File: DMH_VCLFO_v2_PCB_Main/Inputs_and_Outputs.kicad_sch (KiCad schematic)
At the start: 61 parts, among them J1 TS_Jack_6.35mm_Sw, J10 IDC_02x05, J19 Conn_01x08, J2 TS_Jack_6.35mm_Sw, J3 TS_Jack_6.35mm_Sw, J4 TS_Jack_6.35mm_Sw, J5 TS_Jack_6.35mm_Sw, J6 TS_Jack_6.35mm_Sw, J7 Conn_01x08, J8 Conn_01x08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

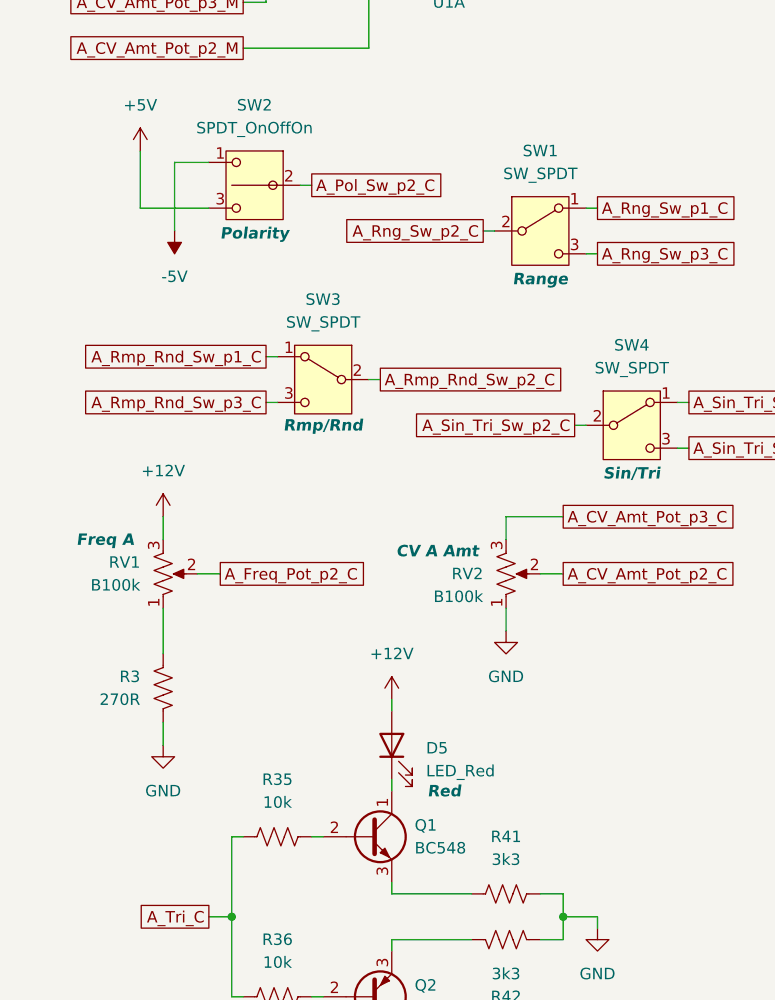
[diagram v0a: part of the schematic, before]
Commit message: Designed osc core based on slew module
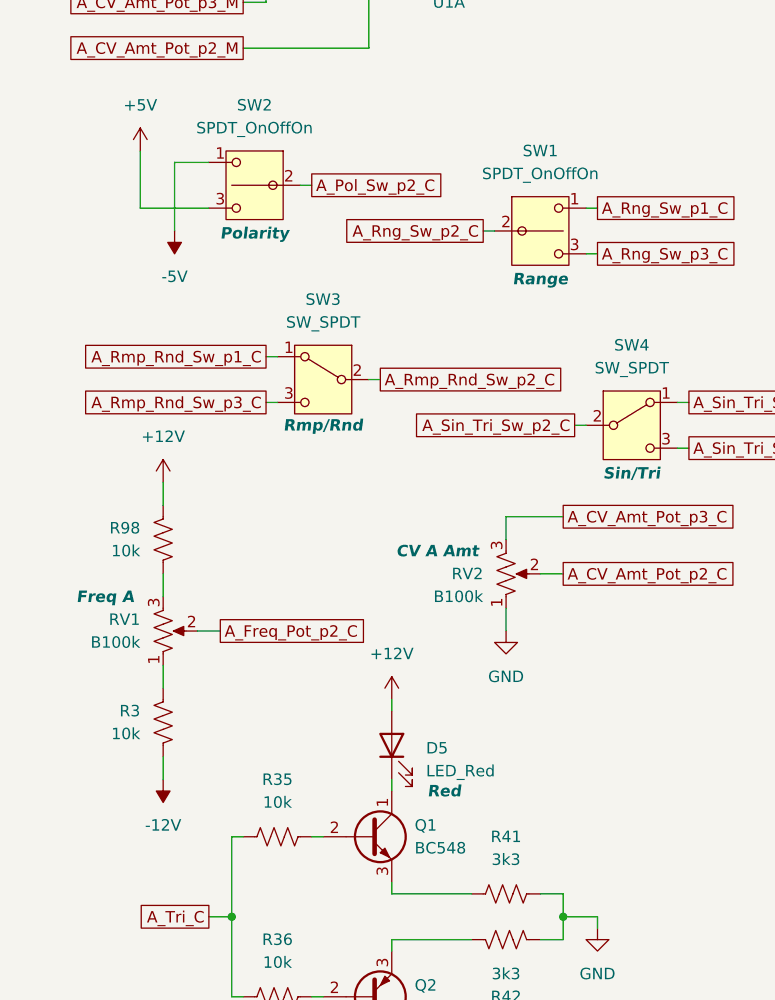
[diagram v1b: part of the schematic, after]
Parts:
- added R98: 10k, Resistor_THT:R_Axial_DIN0207_L6.3mm_D2.5mm_P7.62mm_Horizontal, symbol Device:R_US
- R3: value 270R -> 10k
- SW1: value SW_SPDT -> SPDT_OnOffOn; symbol Switch:SW_SPDT -> SynthStuff:SW_SPDT_OnOffOn
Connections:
- net +12V: now also R98.1; no longer RV1.3
- net -12V: now also R3.2
- net GND: no longer R3.2
- new net: R98.2, RV1.3
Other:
- moved on the sheet: R3, RV1
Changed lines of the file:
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@@
 	(wire
 		(pts
-			(xy 25.4 137.16) (xy 25.4 139.7)
+			(xy 25.4 140.97) (xy 25.4 143.51)
 		)
 		(stroke
@@
 	(wire
 		(pts
+			(xy 25.4 120.65) (xy 25.4 123.19)
+		)
+		(stroke
+			(width 0)
+			(type default)
+		)
+	)
+	(wire
+		(pts
 			(xy 50.8 156.21) (xy 50.8 154.94)
 		)
@@
 	(wire
 		(pts
-			(xy 25.4 114.3) (xy 25.4 116.84)
+			(xy 25.4 110.49) (xy 25.4 113.03)
 		)
 		(stroke
@@
 	(wire
 		(pts
-			(xy 29.21 120.65) (xy 31.75 120.65)
+			(xy 29.21 127) (xy 31.75 127)
 		)
 		(stroke
@@
 	(wire
 		(pts
-			(xy 25.4 124.46) (xy 25.4 129.54)
+			(xy 25.4 130.81) (xy 25.4 133.35)
 		)
 		(stroke
@@
 	(global_label "A_Freq_Pot_p2_C"
 		(shape passive)
-		(at 31.75 120.65 0)
+		(at 31.75 127 0)
 		(fields_autoplaced yes)
 		(effects
@@
 		)
 		(property "Intersheetrefs" "${INTERSHEET_REFS}"
-			(at 49.4685 120.65 0)
+			(at 49.4685 127 0)
 			(effects
 				(font
@@
 	(symbol
 		(lib_id "Device:R_US")
+		(at 25.4 116.84 0)
+		(mirror y)
+		(unit 1)
+		(exclude_from_sim no)
+		(in_bom yes)
+		(on_board no)
+		(dnp no)
+		(property "Reference" "R98"
+			(at 22.86 115.5699 0)
+			(effects
+				(font
+					(size 1.27 1.27)
+				)
+				(justify left)
+			)
+		)
+		(property "Value" "10k"
+			(at 22.86 118.1099 0)
+			(effects
+				(font
+					(size 1.27 1.27)
+				)
+				(justify left)
+			)
+		)
+		(property "Footprint" "Resistor_THT:R_Axial_DIN0207_L6.3mm_D2.5mm_P7.62mm_Horizontal"
+			(at 24.384 117.094 90)
+			(effects
+				(font
+					(size 1.27 1.27)
+				)
+				(hide yes)
+			)
+		)
+		(property "Datasheet" "~"
+			(at 25.4 116.84 0)
+			(effects
+				(font
+					(size 1.27 1.27)
+				)
+				(hide yes)
+			)
+		)
+		(property "Description" "Resistor, US symbol"
+			(at 25.4 116.84 0)
+			(effects
+				(font
+					(size 1.27 1.27)
+				)
+				(hide yes)
+			)
+		)
+		(property "Function" ""
+			(at 25.4 116.84 0)
+			(effects
+				(font
+					(size 1.27 1.27)
+				)
+			)
+		)
+		(pin "1"
+		)
+		(pin "2"
+		)
+		(instances
+			(project "DMH_VCLFO_v2_PCB_Main"
+				(path "/58f4306d-5387-4983-bb08-41a2313fd315/ce3fef8b-9f1d-4178-b50b-4a046c030679"
+					(reference "R98")
+					(unit 1)
+				)
+			)
+		)
+	)
+	(symbol
+		(lib_id "Device:R_US")
 		(at 125.73 139.7 90)
 		(unit 1)
@@
 	)
 	(symbol
-		(lib_id "power:GND")
-		(at 25.4 139.7 0)
-		(unit 1)
-		(exclude_from_sim no)
-		(in_bom yes)
-		(on_board no)
-		(dnp no)
-		(fields_autoplaced yes)
-		(property "Reference" "#PWR019"
-			(at 25.4 146.05 0)
-			(effects
-				(font
-					(size 1.27 1.27)
-				)
-				(hide yes)
-			)
-		)
-		(property "Value" "GND"
-			(at 25.4 144.78 0)
-			(effects
-				(font
-					(size 1.27 1.27)
-				)
-			)
-		)
-		(property "Footprint" ""
-			(at 25.4 139.7 0)
-			(effects
-				(font
-					(size 1.27 1.27)
-				)
-				(hide yes)
-			)
-		)
-		(property "Datasheet" ""
-			(at 25.4 139.7 0)
-			(effects
-				(font
-					(size 1.27 1.27)
-				)
-				(hide yes)
-			)
-		)
-		(property "Description" "Power symbol creates a global label with name \"GND\" , ground"
-			(at 25.4 139.7 0)
-			(effects
-				(font
-					(size 1.27 1.27)
-				)
-				(hide yes)
-			)
-		)
-		(pin "1"
-		)
-		(instances
-			(project "DMH_VCLFO_PCB_1"
-				(path "/58f4306d-5387-4983-bb08-41a2313fd315/ce3fef8b-9f1d-4178-b50b-4a046c030679"
-					(reference "#PWR019")
-					(unit 1)
-				)
-			)
-		)
-	)
-	(symbol
 		(lib_id "Device:R_US")
 		(at 43.18 44.45 90)
@@
 	(symbol
 		(lib_id "Device:R_Potentiometer_US")
-		(at 25.4 120.65 0)
+		(at 25.4 127 0)
 		(mirror x)
 		(unit 1)
@@
 		(dnp no)
 		(property "Reference" "RV1"
-			(at 22.86 119.3799 0)
+			(at 22.86 125.7299 0)
 			(effects
 				(font
@@
 		)
 		(property "Value" "B100k"
-			(at 22.86 121.9199 0)
+			(at 22.86 128.2699 0)
 			(effects
 				(font
@@
 		)
 		(property "Footprint" "SynthStuff:Potentiometer_TT_P110KH1"
-			(at 25.4 120.65 0)
+			(at 25.4 127 0)
 			(effects
 				(font
@@
 		)
 		(property "Datasheet" "~"
-			(at 25.4 120.65 0)
+			(at 25.4 127 0)
 			(effects
 				(font
@@
 		)
 		(property "Description" "Potentiometer, US symbol"
-			(at 25.4 120.65 0)
+			(at 25.4 127 0)
 			(effects
 				(font
@@
 		)
 		(property "Function" "Freq A"
-			(at 15.748 116.84 0)
+			(at 15.748 123.19 0)
 			(effects
 				(font
@@
 	)
 	(symbol
-		(lib_id "Switch:SW_SPDT")
+		(lib_id "SynthStuff:SW_SPDT_OnOffOn")
 		(at 67.31 82.55 0)
 		(unit 1)
@@
 			)
 		)
-		(property "Value" "SW_SPDT"
+		(property "Value" "SPDT_OnOffOn"
 			(at 67.31 76.2 0)
 			(effects
@@
 	(symbol
 		(lib_id "Device:R_US")
-		(at 25.4 133.35 0)
+		(at 25.4 137.16 0)
 		(mirror y)
 		(unit 1)
@@
 		(dnp no)
 		(property "Reference" "R3"
-			(at 22.86 132.0799 0)
+			(at 22.86 135.8899 0)
 			(effects
 				(font
@@
 			)
 		)
-		(property "Value" "270R"
-			(at 22.86 134.6199 0)
+		(property "Value" "10k"
+			(at 22.86 138.4299 0)
 			(effects
 				(font
@@
 		)
 		(property "Footprint" "Resistor_THT:R_Axial_DIN0207_L6.3mm_D2.5mm_P7.62mm_Horizontal"
-			(at 24.384 133.604 90)
+			(at 24.384 137.414 90)
 			(effects
 				(font
@@
 		)
 		(property "Datasheet" "~"
-			(at 25.4 133.35 0)
+			(at 25.4 137.16 0)
 			(effects
 				(font
@@
 		)
 		(property "Description" "Resistor, US symbol"
-			(at 25.4 133.35 0)
+			(at 25.4 137.16 0)
 			(effects
 				(font
@@
 		)
 		(property "Function" ""
-			(at 25.4 133.35 0)
+			(at 25.4 137.16 0)
 			(effects
 				(font
@@
 	)
 	(symbol
+		(lib_id "power:-12V")
+		(at 25.4 143.51 180)
+		(unit 1)
+		(exclude_from_sim no)
+		(in_bom yes)
+		(on_board yes)
+		(dnp no)
+		(fields_autoplaced yes)
+		(property "Reference" "#PWR019"
+			(at 25.4 139.7 0)
+			(effects
+				(font
+					(size 1.27 1.27)
+				)
+				(hide yes)
+			)
+		)
+		(property "Value" "-12V"
+			(at 25.4 148.59 0)
+			(effects
+				(font
+					(size 1.27 1.27)
+				)
+			)
+		)
+		(property "Footprint" ""
+			(at 25.4 143.51 0)
+			(effects
+				(font
+					(size 1.27 1.27)
+				)
+				(hide yes)
+			)
+		)
+		(property "Datasheet" ""
+			(at 25.4 143.51 0)
+			(effects
+				(font
+					(size 1.27 1.27)
+				)
+				(hide yes)
+			)
+		)
+		(property "Description" "Power symbol creates a global label with name \"-12V\""
+			(at 25.4 143.51 0)
+			(effects
+				(font
+					(size 1.27 1.27)
+				)
+				(hide yes)
+			)
+		)
+		(pin "1"
+		)
+		(instances
+			(project "DMH_VCLFO_v2_PCB_Main"
+				(path "/58f4306d-5387-4983-bb08-41a2313fd315/ce3fef8b-9f1d-4178-b50b-4a046c030679"
+					(reference "#PWR019")
+					(unit 1)
+				)
+			)
+		)
+	)
+	(symbol
 		(lib_id "power:GND")
 		(at 36.83 212.09 0)
@@
 	(symbol
 		(lib_id "power:+12V")
-		(at 25.4 114.3 0)
+		(at 25.4 110.49 0)
 		(unit 1)
 		(exclude_from_sim no)
@@
 		(fields_autoplaced yes)
 		(property "Reference" "#PWR012"
-			(at 25.4 118.11 0)
+			(at 25.4 114.3 0)
 			(effects
 				(font
@@
 		)
 		(property "Value" "+12V"
-			(at 25.4 109.22 0)
+			(at 25.4 105.41 0)
 			(effects
 				(font
@@
 		)
 		(property "Footprint" ""
-			(at 25.4 114.3 0)
+			(at 25.4 110.49 0)
 			(effects
 				(font
@@
 		)
 		(property "Datasheet" ""
-			(at 25.4 114.3 0)
+			(at 25.4 110.49 0)
 			(effects
 				(font
@@
 		)
 		(property "Description" "Power symbol creates a global label with name \"+12V\""
-			(at 25.4 114.3 0)
+			(at 25.4 110.49 0)
 			(effects
 				(font

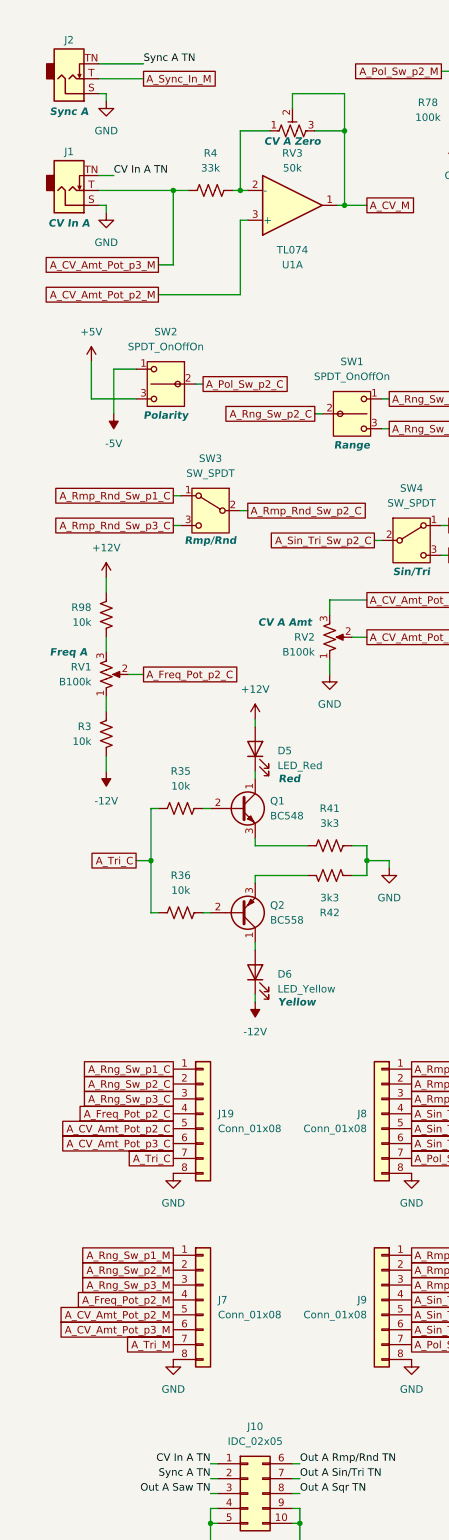
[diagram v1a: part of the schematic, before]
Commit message: Improved inter-PCB connections
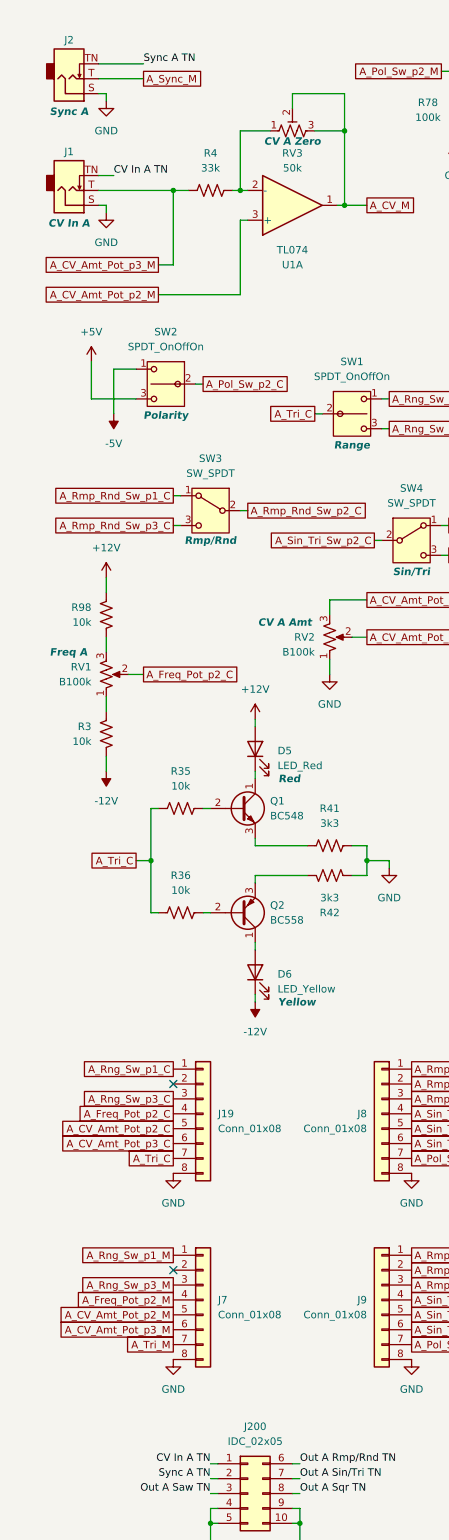
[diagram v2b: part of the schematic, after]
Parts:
- Q1, Q2: footprint Package_TO_SOT_THT:TO-92L_Inline_Wide -> Package_TO_SOT_THT:TO-92_Inline
- renumbered J10 to J200
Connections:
- net A_Tri_C: now also SW1.2 (B)
- net A_Rng_Sw_p2_C: no longer names the net of J19.2 (Pin_2)
- net A_Rng_Sw_p2_C: no longer SW1.2 (B)
- net A_Rng_Sw_p2_M: no longer names the net of J7.2 (Pin_2)
- net A_Sync_In_M renamed A_Sync_M
- no-connect marks 0 -> 2
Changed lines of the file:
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@@
 		(color 0 0 0 0)
 	)
+	(no_connect
+		(at 36.83 228.6)
+	)
+	(no_connect
+		(at 36.83 196.85)
+	)
 	(wire
 		(pts
@@
 		)
 	)
-	(global_label "A_Rng_Sw_p2_C"
-		(shape passive)
-		(at 60.96 82.55 180)
-		(fields_autoplaced yes)
-		(effects
-			(font
-				(size 1.27 1.27)
-			)
-			(justify right)
-		)
-		(property "Intersheetrefs" "${INTERSHEET_REFS}"
-			(at 44.3906 82.55 0)
-			(effects
-				(font
-					(size 1.27 1.27)
-				)
-				(justify right)
-				(hide yes)
-			)
-		)
-	)
 	(global_label "A_CV_M"
 		(shape passive)
@@
 		)
 	)
-	(global_label "A_Rng_Sw_p2_C"
-		(shape passive)
-		(at 36.83 196.85 180)
-		(fields_autoplaced yes)
-		(effects
-			(font
-				(size 1.27 1.27)
-			)
-			(justify right)
-		)
-		(property "Intersheetrefs" "${INTERSHEET_REFS}"
-			(at 20.2606 196.85 0)
-			(effects
-				(font
-					(size 1.27 1.27)
-				)
-				(justify right)
-				(hide yes)
-			)
-		)
-	)
 	(global_label "A_Pol_Sw_p2_C"
 		(shape passive)
@@
 		)
 	)
-	(global_label "A_Rng_Sw_p2_M"
+	(global_label "A_Tri_C"
 		(shape passive)
-		(at 36.83 228.6 180)
+		(at 30.48 158.75 180)
 		(fields_autoplaced yes)
 		(effects
@@
 		)
 		(property "Intersheetrefs" "${INTERSHEET_REFS}"
-			(at 20.0792 228.6 0)
+			(at 21.9537 158.75 0)
 			(effects
 				(font
@@
 		)
 	)
-	(global_label "A_Tri_C"
+	(global_label "A_Rmp_Rnd_Sw_p1_M"
 		(shape passive)
-		(at 30.48 158.75 180)
+		(at 160.02 116.84 0)
 		(fields_autoplaced yes)
 		(effects
@@
 				(size 1.27 1.27)
 			)
-			(justify right)
+			(justify left)
 		)
 		(property "Intersheetrefs" "${INTERSHEET_REFS}"
-			(at 21.9537 158.75 0)
+			(at 181.8507 116.84 0)
 			(effects
 				(font
 					(size 1.27 1.27)
 				)
-				(justify right)
+				(justify left)
 				(hide yes)
 			)
 		)
 	)
-	(global_label "A_Rmp_Rnd_Sw_p1_M"
+	(global_label "A_CV_Amt_Pot_p2_M"
 		(shape passive)
-		(at 160.02 116.84 0)
+		(at 34.29 62.23 180)
 		(fields_autoplaced yes)
 		(effects
@@
 				(size 1.27 1.27)
 			)
-			(justify left)
+			(justify right)
 		)
 		(property "Intersheetrefs" "${INTERSHEET_REFS}"
-			(at 181.8507 116.84 0)
+			(at 13.6687 62.23 0)
 			(effects
 				(font
 					(size 1.27 1.27)
 				)
-				(justify left)
+				(justify right)
 				(hide yes)
 			)
 		)
 	)
-	(global_label "A_CV_Amt_Pot_p2_M"
+	(global_label "A_Tri_C"
 		(shape passive)
-		(at 34.29 62.23 180)
+		(at 60.96 82.55 180)
 		(fields_autoplaced yes)
 		(effects
@@
 		)
 		(property "Intersheetrefs" "${INTERSHEET_REFS}"
-			(at 13.6687 62.23 0)
+			(at 52.4337 82.55 0)
 			(effects
 				(font
@@
 		)
 	)
-	(global_label "A_Sync_In_M"
+	(global_label "A_Sync_M"
 		(shape passive)
 		(at 31.75 25.4 0)
@@
 		)
 		(property "Intersheetrefs" "${INTERSHEET_REFS}"
-			(at 45.2352 25.4 0)
+			(at 42.5138 25.4 0)
 			(effects
 				(font
@@
 		(dnp no)
 		(fields_autoplaced yes)
-		(property "Reference" "J10"
+		(property "Reference" "J200"
 			(at 50.8 255.27 0)
 			(effects
@@
 			(project ""
 				(path "/58f4306d-5387-4983-bb08-41a2313fd315/ce3fef8b-9f1d-4178-b50b-4a046c030679"
-					(reference "J10")
+					(reference "J200")
 					(unit 1)
 				)
@@
 			)
 		)
-		(property "Footprint" "Package_TO_SOT_THT:TO-92L_Inline_Wide"
+		(property "Footprint" "Package_TO_SOT_THT:TO-92_Inline"
 			(at 53.34 151.765 0)
 			(effects
@@
 			)
 		)
+		(property "Sim.Device" "NPN"
+			(at 48.26 149.86 0)
+			(effects
+				(font
+					(size 1.27 1.27)
+				)
+				(hide yes)
+			)
+		)
+		(property "Sim.Pins" "1=C 2=B 3=E"
+			(at 48.26 149.86 0)
+			(effects
+				(font
+					(size 1.27 1.27)
+				)
+				(hide yes)
+			)
+		)
 		(pin "3"
 		)
@@
 			)
 		)
-		(property "Footprint" "Package_TO_SOT_THT:TO-92L_Inline_Wide"
+		(property "Footprint" "Package_TO_SOT_THT:TO-92_Inline"
 			(at 53.34 165.735 0)
 			(effects
@@
 			(at 48.26 167.64 0)
 			(effects
+				(font
+					(size 1.27 1.27)
+				)
+				(hide yes)
+			)
+		)
+		(property "Sim.Device" "PNP"
+			(at 48.26 167.64 0)
+			(effects
+				(font
+					(size 1.27 1.27)
+				)
+				(hide yes)
+			)
+		)
+		(property "Sim.Pins" "1=C 2=B 3=E"
+			(at 48.26 167.64 0)
+			(effects

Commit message: Notes from breadboarding
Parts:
- Q1, Q2: footprint Package_TO_SOT_THT:TO-92_Inline -> Package_TO_SOT_THT:TO-92L_Inline_Wide
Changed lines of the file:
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@@
 			)
 		)
-		(property "Footprint" "Package_TO_SOT_THT:TO-92_Inline"
+		(property "Footprint" "Package_TO_SOT_THT:TO-92L_Inline_Wide"
 			(at 53.34 151.765 0)
 			(effects
@@
 			)
 		)
-		(property "Footprint" "Package_TO_SOT_THT:TO-92_Inline"
+		(property "Footprint" "Package_TO_SOT_THT:TO-92L_Inline_Wide"
 			(at 53.34 165.735 0)
 			(effects

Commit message: Sch redesign in progress
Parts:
- removed R10, R11, R12, R13, R14, R15, R16, R17, R18, R19, R20, R21, R22, R23, R24, R25, R26, R27, R28, R78, R8, R9: 100k, Resistor_THT:R_Axial_DIN0207_L6.3mm_D2.5mm_P7.62mm_Horizontal, symbol Device:R_US
- removed R29, R30, R31, R32, R33, R34: 1k, Resistor_THT:R_Axial_DIN0207_L6.3mm_D2.5mm_P7.62mm_Horizontal, symbol Device:R_US
- removed unit 4 of U1
- removed U2: TL074, Package_DIP:DIP-14_W7.62mm_Socket, symbol Amplifier_Operational:TL074
- R5, R6, R7: value 100k -> 1k
- SW2: Function Polarity -> Bus CV
- U1: footprint Package_DIP:DIP-14_W7.62mm_Socket -> (none)
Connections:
- net A_Rmp_Rnd_Sw_p1_M is gone; now on net A_Rmp_M: J9.1 (Pin_1)
- net A_Rmp_Rnd_Sw_p3_M is gone; now on net A_Rnd_M: J9.3 (Pin_3)
- net A_Sin_Tri_Sw_p1_M is gone; now on net A_Sin_M: J9.4 (Pin_4)
- net A_Sin_Tri_Sw_p3_C is gone; now on net A_Tri_C: J8.6 (Pin_6), SW4.3 (C)
- net A_Sin_Tri_Sw_p3_M is gone; now on net A_Tri_M: J9.6 (Pin_6)
- net A_Rmp_Rnd_Sw_p2_M: now also R7.1; no longer J5.T
- net A_Saw_M: now also R5.1
- net A_Sqr_M: now also U1.10 (+)
- net A_Tri_C: no longer J19.7 (Pin_7)
- net A_Tri_M: no longer J7.7 (Pin_7), R6.1
- net CV In A TN: no longer J200.1 (Pin_1)
- net GND: no longer R7.2
- net at U1.8: now also R6.1, U1.9 (-)
- net at J4.T: now also R5.2
- net at U1.6 (-): no longer R7.1
- net at J3.T: now also R6.2
- net +5V: no longer names the net of SW2.3 (C)
- net -5V: no longer names the net of SW2.1 (A)
- net A_Pol_Sw_p2_C renamed A_BusCV_Sw_p2_C
- net A_Pol_Sw_p2_M renamed A_BusCV_Sw_p2_M
- net A_Rmp_Rnd_Sw_p1_C renamed A_Rmp_C
- net A_Rmp_Rnd_Sw_p3_C renamed A_Rnd_C
- net A_Sin_Tri_Sw_p1_C renamed A_Sin_C
- new net: J5.T, R7.2
- now unconnected: U1.5 (+)
- no-connect marks 2 -> 5
